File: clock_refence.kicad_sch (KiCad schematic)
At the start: 52 parts, among them J204 REFOUT_AUX_P, J205 REFOUT_AUX_N, J206 RFShield_TwoPieces, J207 REFOUT, J209 DNP, T202 TC2-1T+, U201 Si53301, U202 XC6204B33

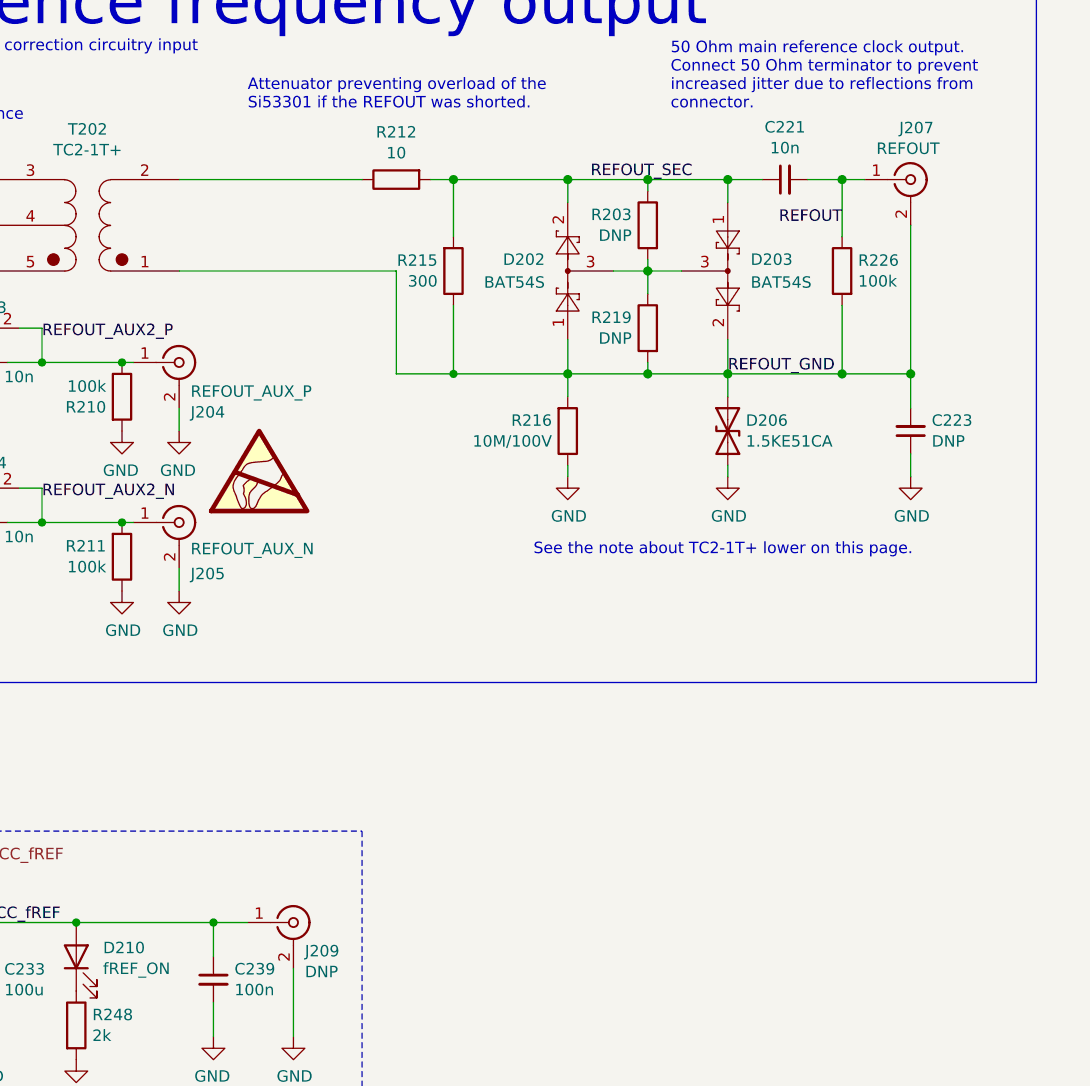
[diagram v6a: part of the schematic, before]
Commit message: Schematic checked. All footprints assigned. Electrolytics need footprint check, so do the RS485 and power connectors and the MuRata oscillator (also it is now EOL) and the crystal. The power protection transils on aux input/output need replacement. PCB in sync with SCH.
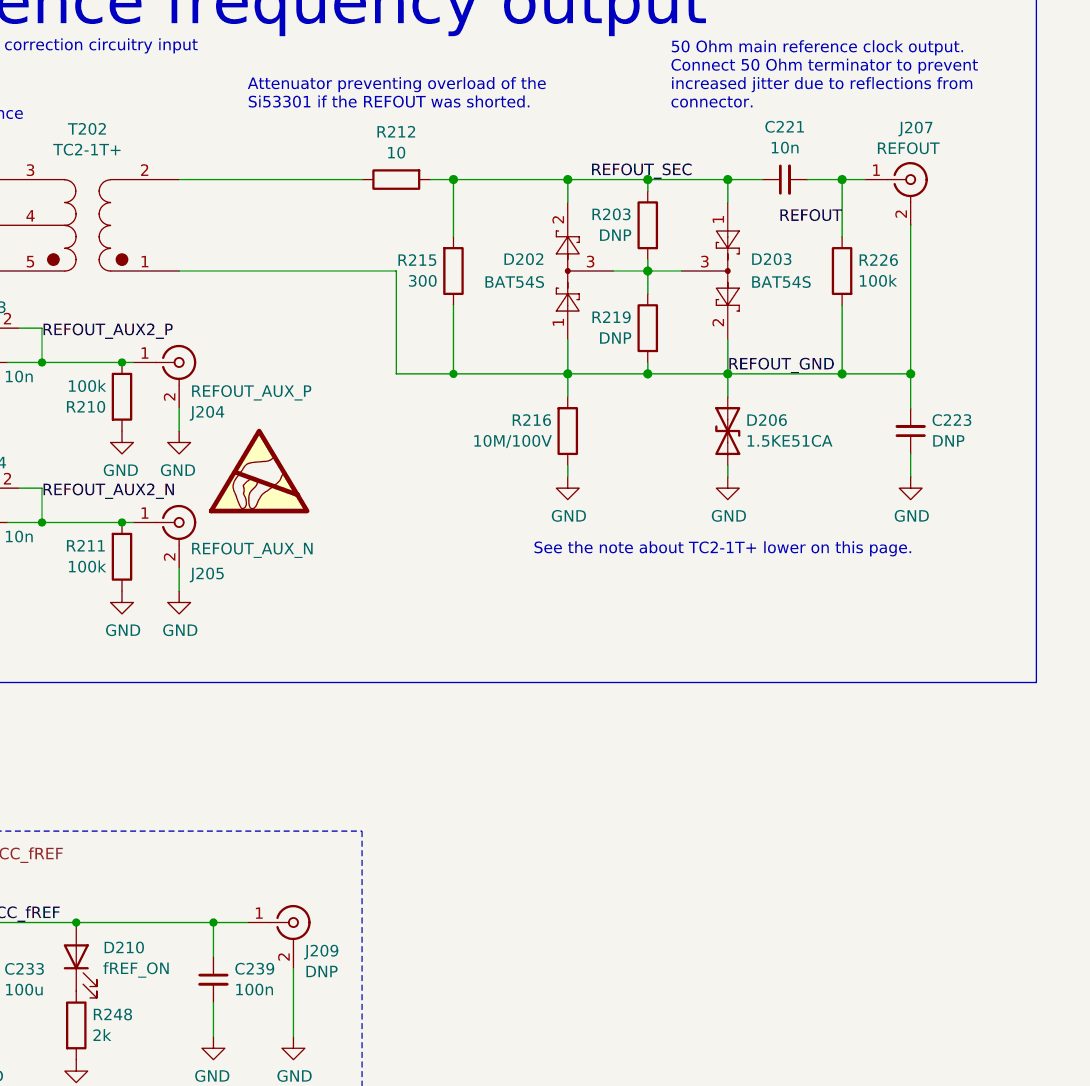
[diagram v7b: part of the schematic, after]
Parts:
- C231: footprint Capacitor_SMD:C_0603_1608Metric_Pad1.08x0.95mm_HandSolder -> Capacitor_SMD:C_0805_2012Metric_Pad1.18x1.45mm_HandSolder
- J206: footprint RF_Shielding:Laird_Technologies_BMI-S-206-F_36.83x33.68mm -> RF_Shielding:Laird_Technologies_BMI-S-205-F_38.10x25.40mm
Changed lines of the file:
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@@
     (comment 3 "Dual channel symmetric outputs")
   )
-  (junction (at 111.76 175.26) (diameter 1.016) (color 0 0 0 0))
+  (junction (at 214.63 114.3) (diameter 1.016) (color 0 0 0 0))
+  (junction (at 64.77 50.8) (diameter 1.016) (color 0 0 0 0))
+  (junction (at 185.42 114.3) (diameter 1.016) (color 0 0 0 0))
+  (junction (at 99.06 50.8) (diameter 0.9144) (color 0 0 0 0))
+  (junction (at 121.92 175.26) (diameter 0.9144) (color 0 0 0 0))
   (junction (at 29.21 175.26) (diameter 1.016) (color 0 0 0 0))
   (junction (at 118.11 130.81) (diameter 0.9144) (color 0 0 0 0))
-  (junction (at 127 130.81) (diameter 0.9144) (color 0 0 0 0))
   (junction (at 55.88 50.8) (diameter 0.9144) (color 0 0 0 0))
+  (junction (at 105.41 113.03) (diameter 0.9144) (color 0 0 0 0))
+  (junction (at 118.11 113.03) (diameter 0.9144) (color 0 0 0 0))
+  (junction (at 102.87 175.26) (diameter 1.016) (color 0 0 0 0))
+  (junction (at 20.32 175.26) (diameter 1.016) (color 0 0 0 0))
+  (junction (at 163.83 92.71) (diameter 1.016) (color 0 0 0 0))
+  (junction (at 109.22 50.8) (diameter 1.016) (color 0 0 0 0))
+  (junction (at 185.42 92.71) (diameter 1.016) (color 0 0 0 0))
+  (junction (at 63.5 179.07) (diameter 1.016) (color 0 0 0 0))
+  (junction (at 93.98 175.26) (diameter 1.016) (color 0 0 0 0))
+  (junction (at 137.16 175.26) (diameter 0.9144) (color 0 0 0 0))
+  (junction (at 194.31 114.3) (diameter 1.016) (color 0 0 0 0))
   (junction (at 127 113.03) (diameter 0.9144) (color 0 0 0 0))
   (junction (at 207.01 92.71) (diameter 1.016) (color 0 0 0 0))
+  (junction (at 50.8 179.07) (diameter 0.9144) (color 0 0 0 0))
+  (junction (at 111.76 175.26) (diameter 1.016) (color 0 0 0 0))
+  (junction (at 38.1 175.26) (diameter 0.9144) (color 0 0 0 0))
+  (junction (at 207.01 114.3) (diameter 1.016) (color 0 0 0 0))
+  (junction (at 176.53 92.71) (diameter 1.016) (color 0 0 0 0))
   (junction (at 77.47 58.42) (diameter 0.9144) (color 0 0 0 0))
   (junction (at 85.09 50.8) (diameter 1.016) (color 0 0 0 0))
   (junction (at 185.42 102.87) (diameter 1.016) (color 0 0 0 0))
-  (junction (at 64.77 50.8) (diameter 1.016) (color 0 0 0 0))
-  (junction (at 185.42 92.71) (diameter 1.016) (color 0 0 0 0))
-  (junction (at 185.42 114.3) (diameter 1.016) (color 0 0 0 0))
+  (junction (at 127 130.81) (diameter 0.9144) (color 0 0 0 0))
+  (junction (at 194.31 92.71) (diameter 1.016) (color 0 0 0 0))
+  (junction (at 69.85 50.8) (diameter 1.016) (color 0 0 0 0))
   (junction (at 163.83 114.3) (diameter 0.9144) (color 0 0 0 0))
-  (junction (at 109.22 50.8) (diameter 1.016) (color 0 0 0 0))
-  (junction (at 102.87 175.26) (diameter 1.016) (color 0 0 0 0))
-  (junction (at 105.41 113.03) (diameter 0.9144) (color 0 0 0 0))
-  (junction (at 121.92 175.26) (diameter 0.9144) (color 0 0 0 0))
   (junction (at 176.53 114.3) (diameter 1.016) (color 0 0 0 0))
-  (junction (at 118.11 113.03) (diameter 0.9144) (color 0 0 0 0))
-  (junction (at 99.06 50.8) (diameter 0.9144) (color 0 0 0 0))
   (junction (at 105.41 127) (diameter 0.9144) (color 0 0 0 0))
-  (junction (at 69.85 50.8) (diameter 1.016) (color 0 0 0 0))
-  (junction (at 214.63 114.3) (diameter 1.016) (color 0 0 0 0))
-  (junction (at 50.8 179.07) (diameter 0.9144) (color 0 0 0 0))
-  (junction (at 194.31 92.71) (diameter 1.016) (color 0 0 0 0))
-  (junction (at 38.1 175.26) (diameter 0.9144) (color 0 0 0 0))
-  (junction (at 176.53 92.71) (diameter 1.016) (color 0 0 0 0))
-  (junction (at 93.98 175.26) (diameter 1.016) (color 0 0 0 0))
   (junction (at 90.17 50.8) (diameter 1.016) (color 0 0 0 0))
-  (junction (at 163.83 92.71) (diameter 1.016) (color 0 0 0 0))
-  (junction (at 194.31 114.3) (diameter 1.016) (color 0 0 0 0))
-  (junction (at 207.01 114.3) (diameter 1.016) (color 0 0 0 0))
-  (junction (at 63.5 179.07) (diameter 1.016) (color 0 0 0 0))
-  (junction (at 137.16 175.26) (diameter 0.9144) (color 0 0 0 0))
-  (junction (at 20.32 175.26) (diameter 1.016) (color 0 0 0 0))
   (no_connect (at 90.17 109.22))
   (no_connect (at 90.17 106.68))
@@
     (stroke (width 0) (type solid) (color 0 0 0 0))
   )
+  (wire (pts (xy 53.34 179.07) (xy 50.8 179.07))
+    (stroke (width 0) (type solid) (color 0 0 0 0))
+  )
   (wire (pts (xy 50.8 179.07) (xy 50.8 180.34))
     (stroke (width 0) (type solid) (color 0 0 0 0))
   )
-  (wire (pts (xy 53.34 179.07) (xy 50.8 179.07))
-    (stroke (width 0) (type solid) (color 0 0 0 0))
-  )
   (wire (pts (xy 194.31 110.49) (xy 194.31 114.3))
     (stroke (width 0) (type solid) (color 0 0 0 0))
@@
     (stroke (width 0) (type default) (color 0 0 0 0))
   )
+  (polyline (pts (xy 102.87 76.2) (xy 102.87 78.74))
+    (stroke (width 0) (type default) (color 0 0 0 0))
+  )
   (polyline (pts (xy 100.33 76.2) (xy 102.87 76.2))
     (stroke (width 0) (type default) (color 0 0 0 0))
   )
-  (polyline (pts (xy 102.87 76.2) (xy 102.87 78.74))
-    (stroke (width 0) (type default) (color 0 0 0 0))
-  )
   (wire (pts (xy 90.17 86.36) (xy 91.44 86.36))
     (stroke (width 0) (type solid) (color 0 0 0 0))
@@
   (wire (pts (xy 214.63 114.3) (xy 214.63 97.79))
     (stroke (width 0) (type solid) (color 0 0 0 0))
+  )
+  (polyline (pts (xy 153.67 165.1) (xy 153.67 196.85))
+    (stroke (width 0) (type dash) (color 0 0 0 0))
+  )
+  (polyline (pts (xy 12.7 165.1) (xy 12.7 196.85))
+    (stroke (width 0) (type dash) (color 0 0 0 0))
+  )
+  (polyline (pts (xy 153.67 196.85) (xy 12.7 196.85))
+    (stroke (width 0) (type dash) (color 0 0 0 0))
   )
   (polyline (pts (xy 12.7 165.1) (xy 153.67 165.1))
     (stroke (width 0) (type dash) (color 0 0 0 0))
   )
-  (polyline (pts (xy 153.67 196.85) (xy 12.7 196.85))
-    (stroke (width 0) (type dash) (color 0 0 0 0))
-  )
-  (polyline (pts (xy 12.7 165.1) (xy 12.7 196.85))
-    (stroke (width 0) (type dash) (color 0 0 0 0))
-  )
-  (polyline (pts (xy 153.67 165.1) (xy 153.67 196.85))
-    (stroke (width 0) (type dash) (color 0 0 0 0))
-  )
   (wire (pts (xy 20.32 175.26) (xy 20.32 179.07))
     (stroke (width 0) (type solid) (color 0 0 0 0))
@@
     (stroke (width 0) (type solid) (color 0 0 0 0))
   )
+  (wire (pts (xy 118.11 109.22) (xy 115.57 109.22))
+    (stroke (width 0) (type solid) (color 0 0 0 0))
+  )
   (wire (pts (xy 118.11 113.03) (xy 118.11 109.22))
     (stroke (width 0) (type solid) (color 0 0 0 0))
   )
-  (wire (pts (xy 118.11 109.22) (xy 115.57 109.22))
-    (stroke (width 0) (type solid) (color 0 0 0 0))
-  )
   (wire (pts (xy 118.11 130.81) (xy 127 130.81))
     (stroke (width 0) (type solid) (color 0 0 0 0))
@@
     (stroke (width 0) (type solid) (color 0 0 0 0))
   )
+  (wire (pts (xy 109.22 113.03) (xy 105.41 113.03))
+    (stroke (width 0) (type solid) (color 0 0 0 0))
+  )
   (wire (pts (xy 105.41 113.03) (xy 105.41 109.22))
     (stroke (width 0) (type solid) (color 0 0 0 0))
   )
-  (wire (pts (xy 109.22 113.03) (xy 105.41 113.03))
-    (stroke (width 0) (type solid) (color 0 0 0 0))
-  )
   (wire (pts (xy 161.29 92.71) (xy 163.83 92.71))
     (stroke (width 0) (type solid) (color 0 0 0 0))
@@
     (stroke (width 0) (type default) (color 0 0 0 0))
   )
+  (polyline (pts (xy 228.6 148.59) (xy 31.75 148.59))
+    (stroke (width 0) (type default) (color 0 0 0 0))
+  )
+  (polyline (pts (xy 31.75 22.86) (xy 228.6 22.86))
+    (stroke (width 0) (type default) (color 0 0 0 0))
+  )
   (polyline (pts (xy 228.6 22.86) (xy 228.6 148.59))
     (stroke (width 0) (type default) (color 0 0 0 0))
   )
-  (polyline (pts (xy 228.6 148.59) (xy 31.75 148.59))
-    (stroke (width 0) (type default) (color 0 0 0 0))
-  )
-  (polyline (pts (xy 31.75 22.86) (xy 228.6 22.86))
-    (stroke (width 0) (type default) (color 0 0 0 0))
-  )
   (wire (pts (xy 63.5 101.6) (xy 64.77 101.6))
     (stroke (width 0) (type solid) (color 0 0 0 0))
@@
     (stroke (width 0) (type solid) (color 0 0 0 0))
   )
+  (wire (pts (xy 185.42 92.71) (xy 194.31 92.71))
+    (stroke (width 0) (type solid) (color 0 0 0 0))
+  )
   (wire (pts (xy 176.53 92.71) (xy 185.42 92.71))
-    (stroke (width 0) (type solid) (color 0 0 0 0))
-  )
-  (wire (pts (xy 185.42 92.71) (xy 194.31 92.71))
     (stroke (width 0) (type solid) (color 0 0 0 0))
   )
@@
       (effects (font (size 1.27 1.27)) (justify left))
     )
-    (property "Footprint" "Capacitor_SMD:C_0603_1608Metric_Pad1.08x0.95mm_HandSolder" (id 2) (at 102.87 181.61 0)
+    (property "Footprint" "Capacitor_SMD:C_0805_2012Metric_Pad1.18x1.45mm_HandSolder" (id 2) (at 102.87 181.61 0)
       (effects (font (size 1.27 1.27)) hide)
     )
@@
     (property "Reference" "J206" (id 0) (at 265.557 133.6356 0))
     (property "Value" "RFShield_TwoPieces" (id 1) (at 265.557 135.9343 0))
-    (property "Footprint" "RF_Shielding:Laird_Technologies_BMI-S-206-F_36.83x33.68mm" (id 2) (at 265.557 151.8158 0)
-      (effects (font (size 1.27 1.27)) hide)
-    )
+    (property "Footprint" "RF_Shielding:Laird_Technologies_BMI-S-205-F_38.10x25.40mm" (id 2) (at 265.557 151.8158 0)
+      (effects (font (size 1.27 1.27)) hide)
+    )
